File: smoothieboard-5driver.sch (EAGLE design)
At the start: 271 parts, among them IC1 LPC1769, IC10 LM1117-3.3V, IC11 78L12F, IC12 A4982, IC2 A4982, IC3 A4982, IC4 MCP44X1, IC5 A4982, IC6 A4982, IC9 MCP44X1, J10 POWER_JACKSMD, Q1 BSL207SP, Q2 12MHz, Q3 25MHz, Q4 ZXMN4A06, Q5 AOT240L, Q6 AOT240L, Q7 AOT240L, Q8 ZXMN4A06, Q9 ZXMN4A06, U1 USD-SOCKETNEW, X14 USBPTH

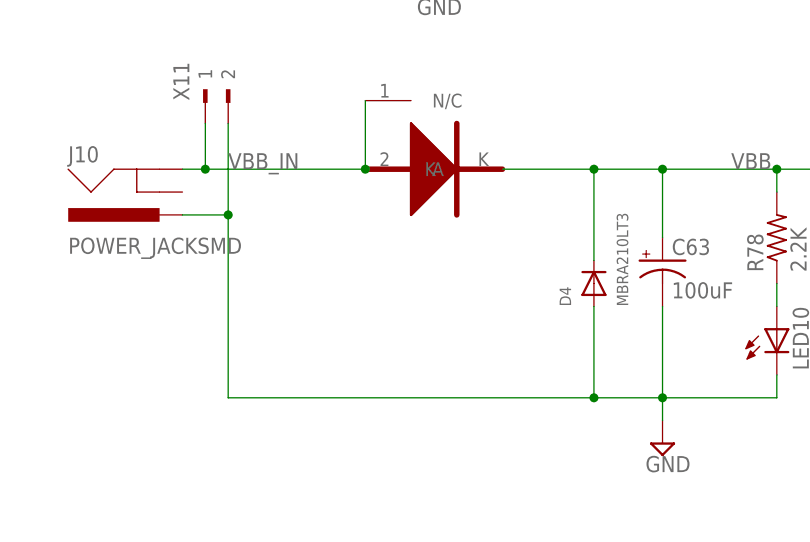
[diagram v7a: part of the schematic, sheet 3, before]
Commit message: Alternative reverse polarity protection using a P-MOSFET. Do not populate both P-MOSFET and Diode footprints, the parts overlap
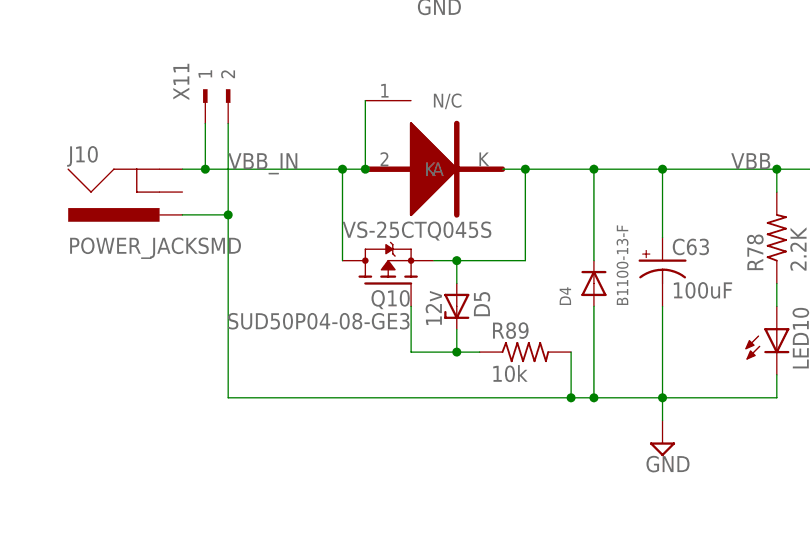
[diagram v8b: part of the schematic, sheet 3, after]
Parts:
- added D5: 12v, diode:ZENER-DIODESMB
- added Q10: SUD50P04-08-GE3, transistor-fet:SPD30P06PTO252
- added R89: 10k, resistor:R-US_R0603
- D4: value MBRA210LT3 -> B1100-13-F
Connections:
- new net N$111: D5.C, Q10.G, R89.1
- net GND: now also R89.2
- net VBB: now also D5.A, Q10.S
- net VBB_IN: now also Q10.D
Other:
- note added: "VS-25CTQ045S"
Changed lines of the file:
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@@
 <part name="U$9" library="eric_sorensen" deviceset="5MMCONN" device=""/>
 <part name="R88" library="resistor" deviceset="R-US_" device="R0603" value="22R"/>
-<part name="D4" library="microbuilder" deviceset="DIODE" device="SMA" value="MBRA210LT3"/>
+<part name="D4" library="microbuilder" deviceset="DIODE" device="SMA" value="B1100-13-F"/>
+<part name="Q10" library="transistor-fet" deviceset="SPD30P06P" device="TO252" value="SUD50P04-08-GE3"/>
+<part name="R89" library="resistor" deviceset="R-US_" device="R0603" value="10k"/>
+<part name="D5" library="diode" deviceset="ZENER-DIODE" device="SMB" value="12v"/>
 </parts>
 <sheets>
@@
 <text x="298.958" y="5.08" size="2.1844" layer="94">http://smoothieware.org</text>
 <rectangle x1="342.265" y1="4.445" x2="382.905" y2="8.255" layer="210"/>
+<text x="139.7" y="35.56" size="1.778" layer="96">VS-25CTQ045S</text>
 </plain>
 <instances>
@@
 <instance part="X10" gate="G$1" x="304.8" y="88.9" rot="MR180"/>
 <instance part="X6" gate="G$1" x="223.52" y="127" rot="R90"/>
-<instance part="D3" gate="G$1" x="144.78" y="45.72" rot="R270"/>
+<instance part="D3" gate="G$1" x="144.78" y="45.72" smashed="yes" rot="R270"/>
 <instance part="JP28" gate="A" x="254" y="129.54"/>
 <instance part="JP11" gate="A" x="312.42" y="137.16"/>
@@
 <instance part="U$6" gate="G$1" x="340.36" y="91.44" rot="MR180"/>
 <instance part="D4" gate="G$1" x="167.64" y="30.48" rot="R90"/>
+<instance part="Q10" gate="G$1" x="144.78" y="30.48" smashed="yes" rot="MR90">
+<attribute name="VALUE" x="147.32" y="25.4" size="1.778" layer="96" rot="MR0"/>
+<attribute name="NAME" x="147.32" y="27.94" size="1.778" layer="95" rot="MR0"/>
+</instance>
+<instance part="R89" gate="G$1" x="160.02" y="22.86"/>
+<instance part="D5" gate="G$1" x="152.4" y="27.94" rot="R270"/>
 </instances>
 <busses>
@@
 <wire x1="127" y1="38.1" x2="127" y2="17.78" width="0.1524" layer="91"/>
 <wire x1="175.26" y1="17.78" x2="167.64" y2="17.78" width="0.1524" layer="91"/>
-<wire x1="167.64" y1="17.78" x2="127" y2="17.78" width="0.1524" layer="91"/>
+<wire x1="167.64" y1="17.78" x2="165.1" y2="17.78" width="0.1524" layer="91"/>
+<wire x1="165.1" y1="17.78" x2="127" y2="17.78" width="0.1524" layer="91"/>
 <wire x1="127" y1="48.26" x2="127" y2="38.1" width="0.1524" layer="91"/>
 <junction x="175.26" y="17.78"/>
@@
 <wire x1="167.64" y1="27.94" x2="167.64" y2="17.78" width="0.1524" layer="91"/>
 <junction x="167.64" y="17.78"/>
+<pinref part="R89" gate="G$1" pin="2"/>
+<wire x1="165.1" y1="22.86" x2="165.1" y2="17.78" width="0.1524" layer="91"/>
+<junction x="165.1" y="17.78"/>
 </segment>
 <segment>
@@
 <wire x1="187.96" y1="43.18" x2="205.74" y2="43.18" width="0.1524" layer="91"/>
 <wire x1="175.26" y1="35.56" x2="175.26" y2="43.18" width="0.1524" layer="91"/>
-<wire x1="157.48" y1="43.18" x2="167.64" y2="43.18" width="0.1524" layer="91"/>
+<wire x1="157.48" y1="43.18" x2="160.02" y2="43.18" width="0.1524" layer="91"/>
+<wire x1="160.02" y1="43.18" x2="167.64" y2="43.18" width="0.1524" layer="91"/>
 <wire x1="167.64" y1="43.18" x2="175.26" y2="43.18" width="0.1524" layer="91"/>
 <wire x1="187.96" y1="40.64" x2="187.96" y2="43.18" width="0.1524" layer="91"/>
@@
 <wire x1="167.64" y1="33.02" x2="167.64" y2="43.18" width="0.1524" layer="91"/>
 <junction x="167.64" y="43.18"/>
+<pinref part="Q10" gate="G$1" pin="S"/>
+<wire x1="149.86" y1="33.02" x2="152.4" y2="33.02" width="0.1524" layer="91"/>
+<wire x1="152.4" y1="33.02" x2="160.02" y2="33.02" width="0.1524" layer="91"/>
+<wire x1="160.02" y1="33.02" x2="160.02" y2="43.18" width="0.1524" layer="91"/>
+<junction x="160.02" y="43.18"/>
+<pinref part="D5" gate="G$1" pin="A"/>
+<wire x1="152.4" y1="30.48" x2="152.4" y2="33.02" width="0.1524" layer="91"/>
+<junction x="152.4" y="33.02"/>
 </segment>
 <segment>
@@
 <net name="VBB_IN" class="0">
 <segment>
-<wire x1="142.24" y1="43.18" x2="124.46" y2="43.18" width="0.1524" layer="91"/>
+<wire x1="142.24" y1="43.18" x2="139.7" y2="43.18" width="0.1524" layer="91"/>
+<wire x1="139.7" y1="43.18" x2="124.46" y2="43.18" width="0.1524" layer="91"/>
 <wire x1="124.46" y1="43.18" x2="121.92" y2="43.18" width="0.1524" layer="91"/>
 <wire x1="124.46" y1="48.26" x2="124.46" y2="43.18" width="0.1524" layer="91"/>
@@
 <wire x1="142.24" y1="43.18" x2="142.24" y2="50.8" width="0.1524" layer="91"/>
 <junction x="142.24" y="43.18"/>
+<pinref part="Q10" gate="G$1" pin="D"/>
+<wire x1="139.7" y1="33.02" x2="139.7" y2="43.18" width="0.1524" layer="91"/>
+<junction x="139.7" y="43.18"/>
 </segment>
 <segment>
@@
 </segment>
 </net>
+<net name="N$111" class="0">
+<segment>
+<pinref part="R89" gate="G$1" pin="1"/>
+<pinref part="Q10" gate="G$1" pin="G"/>
+<wire x1="154.94" y1="22.86" x2="152.4" y2="22.86" width="0.1524" layer="91"/>
+<wire x1="152.4" y1="22.86" x2="147.32" y2="22.86" width="0.1524" layer="91"/>
+<wire x1="147.32" y1="22.86" x2="147.32" y2="27.94" width="0.1524" layer="91"/>
+<pinref part="D5" gate="G$1" pin="C"/>
+<wire x1="152.4" y1="25.4" x2="152.4" y2="22.86" width="0.1524" layer="91"/>
+<junction x="152.4" y="22.86"/>
+</segment>
+</net>
